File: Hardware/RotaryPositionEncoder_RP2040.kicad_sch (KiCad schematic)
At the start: 69 parts, among them J1 Conn_ABI, J2 Conn_USB, J2 Conn_UVW, J5 Conn_5VDC, J7 Conn_CAN, J8 Conn_CAN, J9 Conn_01x04_MountingPin, U1 AS5047P, U2 RP2040, U3 M24C02-RMN, U3 RT9013-33GB, U5 TJA1042T, U7 MAX14783ExS, U8 W25Q32JVZP, Y2 Crystal_GND2

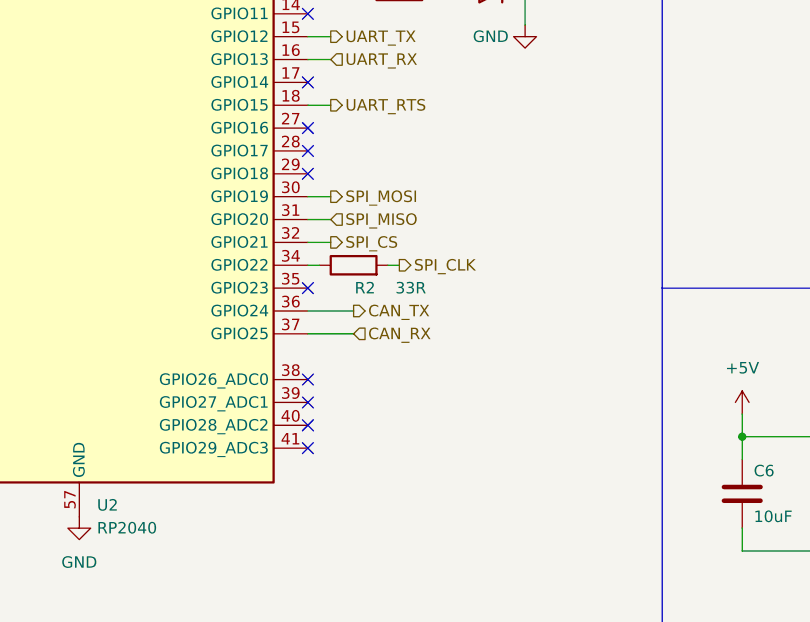
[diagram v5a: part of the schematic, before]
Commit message: Layout almost done Todo: Change QFN56 footprint into handsolder
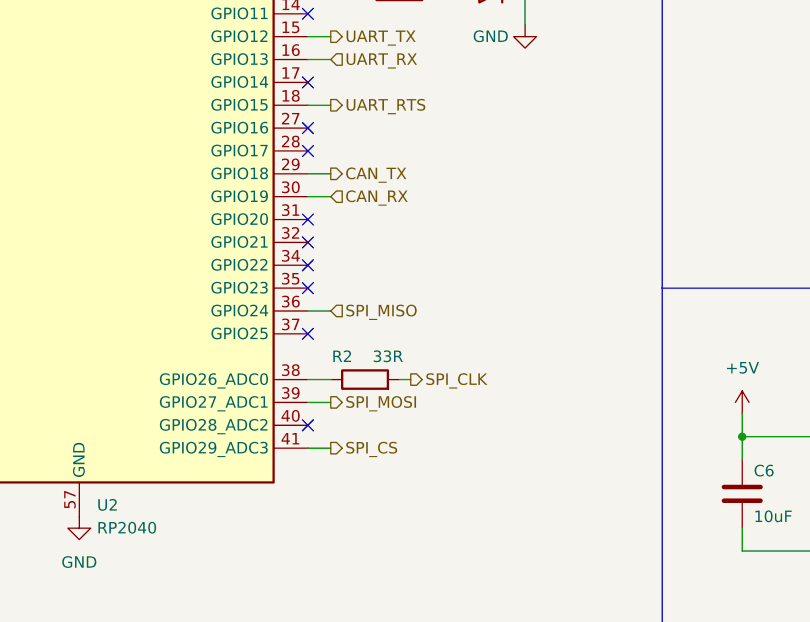
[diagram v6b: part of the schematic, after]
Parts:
- C12, C15: footprint Capacitor_SMD:C_0603_1608Metric -> Capacitor_SMD:C_0805_2012Metric
- H1, H2, H3, H4: footprint MountingHole:MountingHole_3.2mm_M3_Pad_Via -> MountingHole:MountingHole_2.2mm_M2_Pad_TopBottom
- J1, J2: footprint Connector_JST:JST_GH_BM04B-GHS-TBT_1x04-1MP_P1.25mm_Vertical -> Connector_PinHeader_1.27mm:PinHeader_1x04_P1.27mm_Vertical
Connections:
- net CAN_RX: now also U2.30 (GPIO19); no longer U2.37 (GPIO25)
- net CAN_TX: now also U2.29 (GPIO18); no longer U2.36 (GPIO24)
- net SPI_CS: now also U2.41 (GPIO29_ADC3); no longer U2.32 (GPIO21)
- net SPI_MISO: now also U2.36 (GPIO24); no longer U2.31 (GPIO20)
- net SPI_MOSI: now also U2.39 (GPIO27_ADC1); no longer U2.30 (GPIO19)
- net at U2.34 (GPIO22): no longer R2.1
- net at U2.38 (GPIO26_ADC0): now also R2.1
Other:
- moved on the sheet: R2
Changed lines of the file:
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@@
   )
   (no_connect (at 189.23 67.31))
-  (no_connect (at 189.23 115.57))
   (no_connect (at 189.23 97.79))
-  (no_connect (at 189.23 107.95))
   (no_connect (at 189.23 57.15))
+  (no_connect (at 189.23 92.71))
   (no_connect (at 189.23 80.01))
   (no_connect (at 123.19 102.87))
@@
   (no_connect (at 189.23 39.37))
   (no_connect (at 189.23 54.61))
-  (no_connect (at 189.23 85.09))
+  (no_connect (at 189.23 102.87))
   (no_connect (at 189.23 52.07))
   (no_connect (at 172.72 172.72))
   (no_connect (at 189.23 74.93))
-  (no_connect (at 189.23 110.49))
   (no_connect (at 189.23 49.53))
   (no_connect (at 189.23 41.91))
   (no_connect (at 172.72 185.42))
-  (no_connect (at 189.23 82.55))
+  (no_connect (at 189.23 90.17))
   (no_connect (at 118.11 97.79))
+  (no_connect (at 189.23 95.25))
   (no_connect (at 189.23 113.03))
   (no_connect (at 172.72 191.77))
+  (no_connect (at 189.23 82.55))
   (wire (pts (xy 149.86 22.86) (xy 149.86 24.13))
     (stroke (width 0) (type default))
@@
     (stroke (width 0) (type default))
   )
+  (wire (pts (xy 189.23 110.49) (xy 191.77 110.49))
+    (stroke (width 0) (type default))
+  )
   (wire (pts (xy 54.61 105.41) (xy 57.15 105.41))
     (stroke (width 0) (type default))
@@
     (stroke (width 0) (type default))
   )
+  (wire (pts (xy 189.23 85.09) (xy 191.77 85.09))
+    (stroke (width 0) (type default))
+  )
   (wire (pts (xy 59.69 143.51) (xy 59.69 149.86))
     (stroke (width 0) (type default))
@@
     (stroke (width 0) (type default))
   )
-  (wire (pts (xy 191.77 87.63) (xy 189.23 87.63))
-    (stroke (width 0) (type default))
-  )
   (wire (pts (xy 59.69 149.86) (xy 48.26 149.86))
     (stroke (width 0) (type default))
@@
     (stroke (width 0) (type default))
   )
-  (wire (pts (xy 189.23 102.87) (xy 194.31 102.87))
-    (stroke (width 0) (type default))
-  )
   (wire (pts (xy 30.48 102.87) (xy 45.72 102.87))
     (stroke (width 0) (type default))
@@
     (stroke (width 0) (type default))
   )
-  (wire (pts (xy 198.12 95.25) (xy 199.39 95.25))
+  (wire (pts (xy 199.39 107.95) (xy 200.66 107.95))
     (stroke (width 0) (type default))
   )
@@
     (stroke (width 0) (type default))
   )
+  (wire (pts (xy 189.23 100.33) (xy 191.77 100.33))
+    (stroke (width 0) (type default))
+  )
   (wire (pts (xy 144.78 33.02) (xy 149.86 33.02))
     (stroke (width 0) (type default))
@@
     (stroke (width 0) (type default))
   )
-  (wire (pts (xy 189.23 92.71) (xy 191.77 92.71))
-    (stroke (width 0) (type default))
-  )
   (wire (pts (xy 119.38 78.74) (xy 119.38 77.47))
     (stroke (width 0) (type default))
@@
     (stroke (width 0) (type default))
   )
-  (wire (pts (xy 189.23 100.33) (xy 194.31 100.33))
-    (stroke (width 0) (type default))
-  )
   (wire (pts (xy 189.23 77.47) (xy 191.77 77.47))
     (stroke (width 0) (type default))
@@
     (stroke (width 0) (type default))
   )
-  (wire (pts (xy 190.5 95.25) (xy 189.23 95.25))
-    (stroke (width 0) (type default))
-  )
   (wire (pts (xy 21.59 53.34) (xy 26.67 53.34))
     (stroke (width 0) (type default))
@@
     (stroke (width 0) (type default))
   )
+  (wire (pts (xy 191.77 107.95) (xy 189.23 107.95))
+    (stroke (width 0) (type default))
+  )
   (wire (pts (xy 118.11 85.09) (xy 138.43 85.09))
     (stroke (width 0) (type default))
@@
     (stroke (width 0) (type default))
   )
+  (wire (pts (xy 189.23 115.57) (xy 191.77 115.57))
+    (stroke (width 0) (type default))
+  )
   (wire (pts (xy 26.67 44.45) (xy 26.67 41.91))
     (stroke (width 0) (type default))
@@
     (stroke (width 0) (type default))
   )
+  (wire (pts (xy 189.23 87.63) (xy 191.77 87.63))
+    (stroke (width 0) (type default))
+  )
   (wire (pts (xy 22.86 102.87) (xy 30.48 102.87))
     (stroke (width 0) (type default))
@@
     (stroke (width 0) (type default))
   )
-  (wire (pts (xy 191.77 90.17) (xy 189.23 90.17))
-    (stroke (width 0) (type default))
-  )
   (wire (pts (xy 186.69 22.86) (xy 186.69 24.13))
     (stroke (width 0) (type default))
@@
     (effects (font (size 1.27 1.27)) (justify right))
   )
-  (hierarchical_label "CAN_TX" (shape output) (at 194.31 100.33 0) (fields_autoplaced)
-    (effects (font (size 1.27 1.27)) (justify left))
-  )
   (hierarchical_label "CAN_RX" (shape output) (at 31.75 88.9 180) (fields_autoplaced)
     (effects (font (size 1.27 1.27)) (justify right))
@@
     (effects (font (size 1.27 1.27)) (justify left))
   )
-  (hierarchical_label "SPI_CS" (shape output) (at 191.77 92.71 0) (fields_autoplaced)
+  (hierarchical_label "SPI_CS" (shape output) (at 191.77 115.57 0) (fields_autoplaced)
     (effects (font (size 1.27 1.27)) (justify left))
   )
@@
     (effects (font (size 1.27 1.27)) (justify left))
   )
+  (hierarchical_label "CAN_RX" (shape input) (at 191.77 87.63 0) (fields_autoplaced)
+    (effects (font (size 1.27 1.27)) (justify left))
+  )
   (hierarchical_label "USB_DP" (shape input) (at 130.81 46.99 180) (fields_autoplaced)
     (effects (font (size 1.27 1.27)) (justify right))
@@
     (effects (font (size 1.27 1.27)) (justify right))
   )
-  (hierarchical_label "SPI_MOSI" (shape output) (at 191.77 87.63 0) (fields_autoplaced)
+  (hierarchical_label "SPI_MOSI" (shape output) (at 191.77 110.49 0) (fields_autoplaced)
     (effects (font (size 1.27 1.27)) (justify left))
   )
-  (hierarchical_label "SPI_CLK" (shape output) (at 199.39 95.25 0) (fields_autoplaced)
+  (hierarchical_label "SPI_CLK" (shape output) (at 200.66 107.95 0) (fields_autoplaced)
     (effects (font (size 1.27 1.27)) (justify left))
   )
-  (hierarchical_label "CAN_RX" (shape input) (at 194.31 102.87 0) (fields_autoplaced)
+  (hierarchical_label "CAN_TX" (shape output) (at 191.77 85.09 0) (fields_autoplaced)
     (effects (font (size 1.27 1.27)) (justify left))
   )
-  (hierarchical_label "SPI_MISO" (shape input) (at 191.77 90.17 0) (fields_autoplaced)
+  (hierarchical_label "SPI_MISO" (shape input) (at 191.77 100.33 0) (fields_autoplaced)
     (effects (font (size 1.27 1.27)) (justify left))
   )
@@
       (effects (font (size 1.27 1.27)))
     )
-    (property "Footprint" "MountingHole:MountingHole_3.2mm_M3_Pad_Via" (at 170.18 179.07 0)
+    (property "Footprint" "MountingHole:MountingHole_2.2mm_M2_Pad_TopBottom" (at 170.18 179.07 0)
       (effects (font (size 1.27 1.27)) hide)
     )
@@
       (effects (font (size 1.27 1.27)))
     )
-    (property "Footprint" "MountingHole:MountingHole_3.2mm_M3_Pad_Via" (at 170.18 185.42 0)
+    (property "Footprint" "MountingHole:MountingHole_2.2mm_M2_Pad_TopBottom" (at 170.18 185.42 0)
       (effects (font (size 1.27 1.27)) hide)
     )
@@
       (effects (font (size 1.27 1.27)) (justify right))
     )
-    (property "Footprint" "Connector_JST:JST_GH_BM04B-GHS-TBT_1x04-1MP_P1.25mm_Vertical" (at 69.85 35.56 0)
+    (property "Footprint" "Connector_PinHeader_1.27mm:PinHeader_1x04_P1.27mm_Vertical" (at 69.85 35.56 0)
       (effects (font (size 1.27 1.27)) hide)
     )
@@
     )
   )
-  (symbol (lib_id "Device:R") (at 194.31 95.25 90) (unit 1)
+  (symbol (lib_id "Device:R") (at 195.58 107.95 90) (unit 1)
     (in_bom yes) (on_board yes) (dnp no)
-    (property "Reference" "R2" (at 195.58 97.79 90)
+    (property "Reference" "R2" (at 193.04 105.41 90)
       (effects (font (size 1.27 1.27)))
     )
-    (property "Value" "33R" (at 200.66 97.79 90)
+    (property "Value" "33R" (at 198.12 105.41 90)
       (effects (font (size 1.27 1.27)))
     )
-    (property "Footprint" "Resistor_SMD:R_0603_1608Metric" (at 194.31 97.028 90)
+    (property "Footprint" "Resistor_SMD:R_0603_1608Metric" (at 195.58 109.728 90)
       (effects (font (size 1.27 1.27)) hide)
     )
-    (property "Datasheet" "~" (at 194.31 95.25 0)
+    (property "Datasheet" "~" (at 195.58 107.95 0)
       (effects (font (size 1.27 1.27)) hide)
     )
@@
       (effects (font (size 1.27 1.27)))
     )
-    (property "Footprint" "MountingHole:MountingHole_3.2mm_M3_Pad_Via" (at 170.18 172.72 0)
+    (property "Footprint" "MountingHole:MountingHole_2.2mm_M2_Pad_TopBottom" (at 170.18 172.72 0)
       (effects (font (size 1.27 1.27)) hide)
     )
@@
       (effects (font (size 1.27 1.27)))
     )
-    (property "Footprint" "MountingHole:MountingHole_3.2mm_M3_Pad_Via" (at 170.18 191.77 0)
+    (property "Footprint" "MountingHole:MountingHole_2.2mm_M2_Pad_TopBottom" (at 170.18 191.77 0)
       (effects (font (size 1.27 1.27)) hide)
     )
@@
       (effects (font (size 1.27 1.27)) (justify left))
     )
-    (property "Footprint" "Capacitor_SMD:C_0603_1608Metric" (at 145.7452 24.13 0)
+    (property "Footprint" "Capacitor_SMD:C_0805_2012Metric" (at 145.7452 24.13 0)
       (effects (font (size 1.27 1.27)) hide)
     )
@@
       (effects (font (size 1.27 1.27)) (justify right))
     )
-    (property "Footprint" "Connector_JST:JST_GH_BM04B-GHS-TBT_1x04-1MP_P1.25mm_Vertical" (at 69.85 45.72 0)
+    (property "Footprint" "Connector_PinHeader_1.27mm:PinHeader_1x04_P1.27mm_Vertical" (at 69.85 45.72 0)
       (effects (font (size 1.27 1.27)) hide)
     )
@@
       (effects (font (size 1.27 1.27)) (justify left))
     )
-    (property "Footprint" "Capacitor_SMD:C_0603_1608Metric" (at 211.1248 24.13 0)
+    (property "Footprint" "Capacitor_SMD:C_0805_2012Metric" (at 211.1248 24.13 0)
       (effects (font (size 1.27 1.27)) hide)
     )

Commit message: almost done pcb layout v1
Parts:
- removed R12, R13, R14: 4.7K, Resistor_SMD:R_0603_1608Metric, symbol Device:R
- added R2, R3, R4: 4.7K, Resistor_SMD:R_0603_1608Metric, symbol Device:R
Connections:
- net CAN_H: now also D4.1 (K); no longer D4.2 (K)
- net CAN_L: now also D4.2 (K); no longer D4.1 (K)
- net CAN_RX: now also U2.2 (GPIO0); no longer U2.30 (GPIO19)
- net CAN_TX: now also U2.3 (GPIO1); no longer U2.29 (GPIO18)
- net at D2.2 (A): now also R3.1
- net at D3.2 (A): now also R4.1
- net at U2.31 (GPIO20): now also R4.2
- net at D1.2 (A): now also R2.1
- new net: R2.2, U2.29 (GPIO18)
- new net: R3.2, U2.30 (GPIO19)
- no-connect marks 22 -> 19
